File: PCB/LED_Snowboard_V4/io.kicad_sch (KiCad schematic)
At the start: 12 parts, among them J1 Conn_01x04, J3 Conn_01x04, J4 Conn_01x04, J5 XT60PW-M, J6 XT60PW-M, J7 XT60PW-F, J8 Conn_01x03, J9 Conn_01x03, U2 INA220BIDGSR

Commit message: Transfer PCB To Desktop
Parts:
- added D1, D2, D3: D_Schottky, symbol Device:D_Schottky
- added D4, D5: SD05_SOD323, Diode_SMD:D_SOD-323, symbol Diode:SD05_SOD323
- added J10: Conn_01x05, symbol Connector_Generic:Conn_01x05
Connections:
- net +3V3: now also J9.2 (Pin_2)
- net +5V: now also J10.4 (Pin_4)
- net GND: now also J1.1 (Pin_1), J3.1 (Pin_1), J4.1 (Pin_1), J9.3 (Pin_3), D4.1 (A1), D5.1 (A1), J10.5 (Pin_5)
- net SCL: now also D5.2 (A2)
- net SDA: now also D4.2 (A2)
- net VCC: now also J7.2
- net at J8.1 (Pin_1): now also D1.1 (K)
- net at J8.2 (Pin_2): now also D2.1 (K)
- net at J8.3 (Pin_3): now also D3.1 (K)
- net Sensor: now reaches J9.1 (Pin_1)
- new net CLK: J10.1 (Pin_1)
- new net DT: J10.2 (Pin_2)
- new net SW: J10.3 (Pin_3)

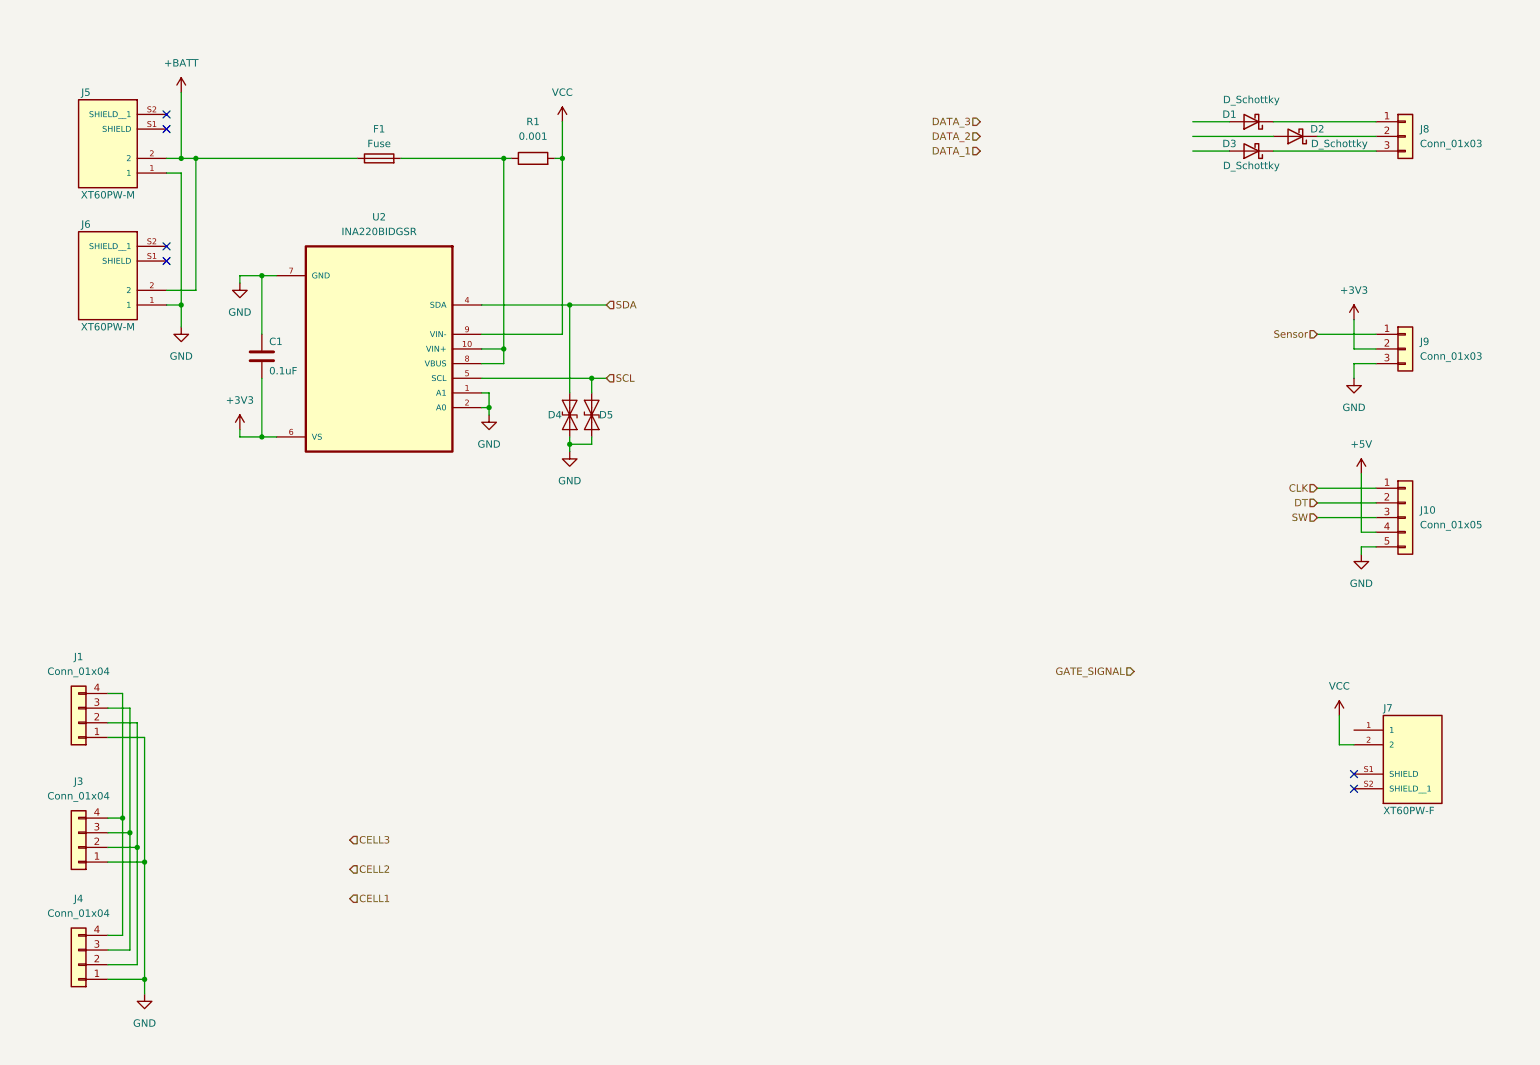
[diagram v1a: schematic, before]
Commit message: Post Review
Reviewed with Tim. need to add power line protections. settled on no battery heater for now
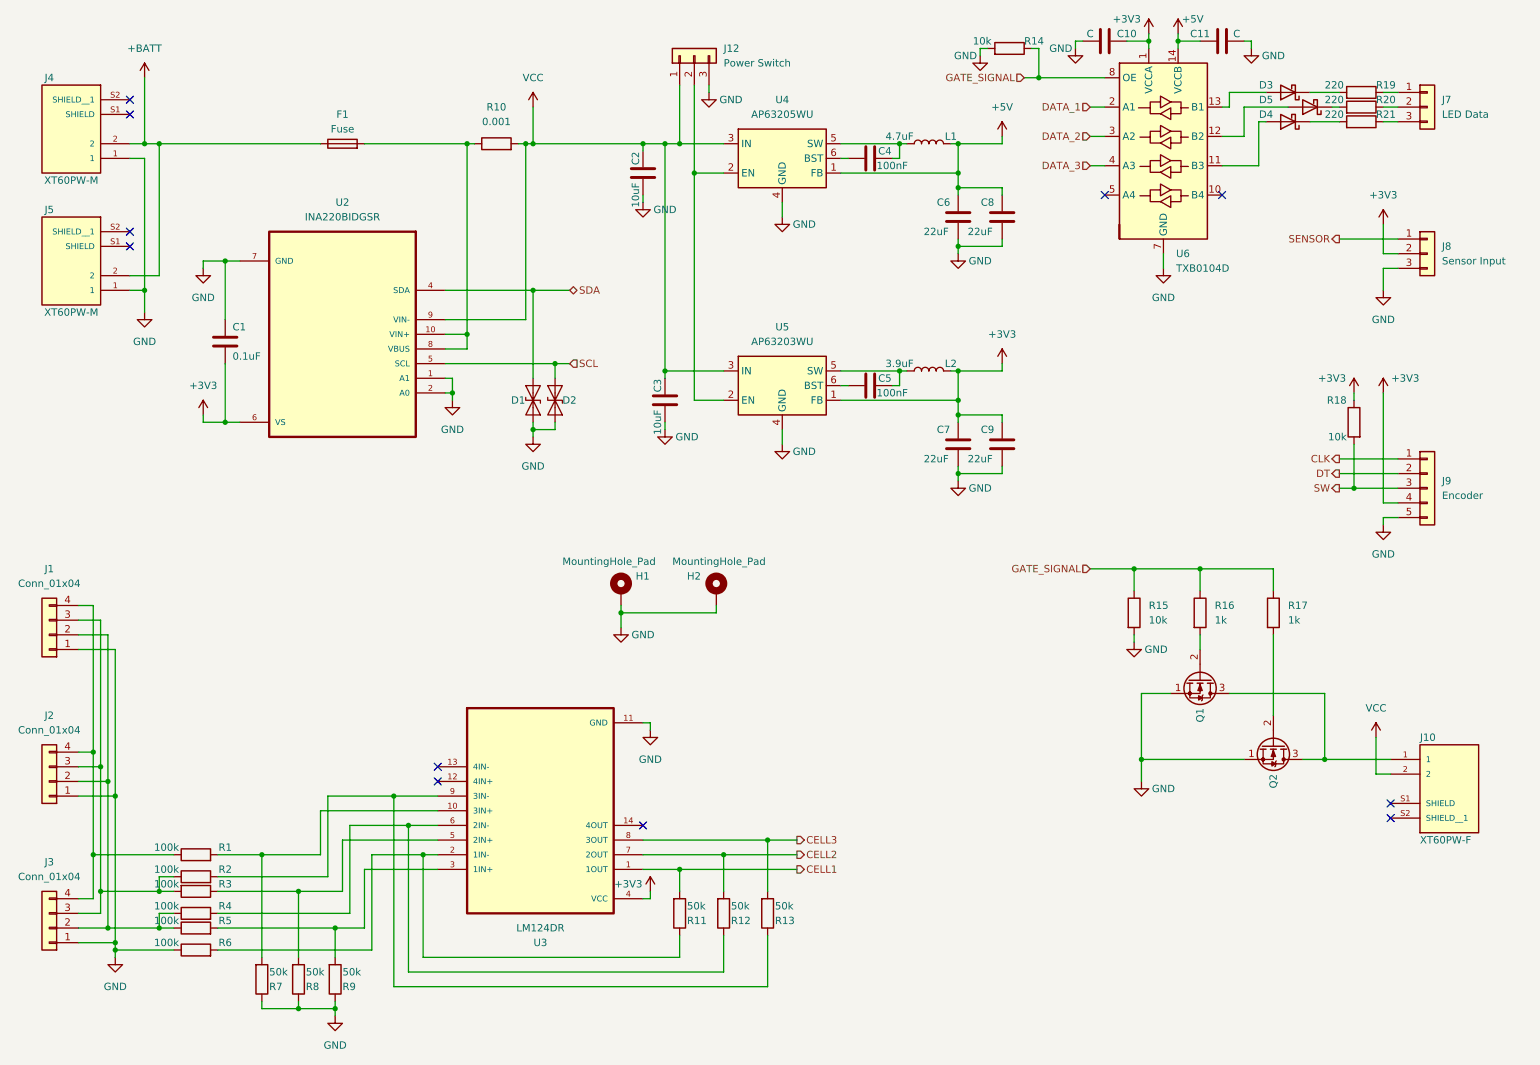
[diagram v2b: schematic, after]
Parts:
- added C10, C11: C, symbol Device:C
- added C2, C3: 10uF, symbol Device:C
- added C4, C5: 100nF, symbol Device:C
- added C6, C7, C8, C9: 22uF, symbol Device:C
- added H1, H2: MountingHole_Pad, symbol Mechanical:MountingHole_Pad
- added J12: Power Switch, symbol Connector_Generic:Conn_01x03
- added L1: 4.7uF, symbol Device:L
- added L2: 3.9uF, symbol Device:L
- added Q1, Q2: ~, symbol Dustins_Symbols:IRFH6200TRPBF
- added R1, R2, R3, R4, R5, R6: 100k, symbol Device:R
- added R11, R12, R13, R7, R8, R9: 50k, symbol Device:R
- added R14, R15, R18: 10k, symbol Device:R
- added R16, R17: 1k, symbol Device:R
- added R19, R20, R21: 220, symbol Device:R
- added U3: LM124DR, SnapEDA Library:SOIC127P600X175-14N, symbol LM124DR:LM124DR
- added U4: AP63205WU, Package_TO_SOT_SMD:TSOT-23-6, symbol Regulator_Switching:AP63205WU
- added U5: AP63203WU, Package_TO_SOT_SMD:TSOT-23-6, symbol Regulator_Switching:AP63203WU
- added U6: TXB0104D, Package_SO:SOIC-14_3.9x8.7mm_P1.27mm, symbol Logic_LevelTranslator:TXB0104D
- J7: renamed from J8; value Conn_01x03 -> LED Data
- J8: renamed from J9; value Conn_01x03 -> Sensor Input
- J9: renamed from J10; value Conn_01x05 -> Encoder
- renumbered D4 to D1, D5 to D2, D1 to D3, D3 to D4, D2 to D5, J7 to J10, J3 to J2, J4 to J3, J5 to J4, J6 to J5, R1 to R10
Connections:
- net +3V3: now also J9.4 (Pin_4), C10.1, C7.2, C9.2, L2.2, R18.1, U3.4 (VCC), U5.1 (FB), U6.1 (VCCA)
- net +5V: now also C11.1, C6.2, C8.2, L1.2, U4.1 (FB), U6.14 (VCCB); no longer J9.4 (Pin_4)
- net CELL1: now also R11.2, U3.1 (1OUT)
- net CELL2: now also R12.2, U3.7 (2OUT)
- net CELL3: now also R13.2, U3.8 (3OUT)
- net DATA_1: now also U6.2 (A1)
- net DATA_2: now also U6.3 (A2)
- net DATA_3: now also U6.4 (A3)
- net GATE_SIGNAL: now also R14.1, R15.1, R16.1, R17.1, U6.8 (OE)
- net GND: now also C10.2, C11.2, C2.1, C3.1, C6.1, C7.1, C8.1, C9.1, H1.1, H2.1, J12.3 (Pin_3), Q1.1 (S), Q2.1 (S), R14.2, R15.2, R6.1, R7.1, R8.1, R9.1, U3.11 (GND), U4.4 (GND), U5.4 (GND), U6.7 (GND)
- net SW: now also R18.2
- net VCC: now also C2.2, C3.2, J12.1 (Pin_1), U4.3 (IN), U5.3 (IN)
- net at J10.1: now also Q1.3 (D), Q2.3 (D)
- net at D3.1 (K): now also R19.2; no longer J7.1 (Pin_1)
- net at D3.2 (A): now also U6.13 (B1)
- net at J7.3 (Pin_3): now also R21.1; no longer D4.1 (K)
- net at D4.2 (A): now also U6.11 (B3)
- net at J7.2 (Pin_2): now also R20.1; no longer D5.1 (K)
- net at D5.2 (A): now also U6.12 (B2)
- net at J1.2 (Pin_2), J2.2 (Pin_2), J3.2 (Pin_2): now also R4.1, R5.1
- net at J1.3 (Pin_3), J2.3 (Pin_3), J3.3 (Pin_3): now also R2.1, R3.2
- net at J1.4 (Pin_4), J2.4 (Pin_4), J3.4 (Pin_4): now also R1.1
- net Sensor renamed SENSOR
- new net: R13.1, R2.2, U3.9 (3IN-)
- new net: R1.2, R7.2, U3.10 (3IN+)
- new net: R11.1, R6.2, U3.2 (1IN-)
- new net: R5.2, R9.2, U3.3 (1IN+)
- new net: R3.1, R8.2, U3.5 (2IN+)
- new net: R12.1, R4.2, U3.6 (2IN-)
- new net: D4.1 (K), R21.2
- new net: Q1.2 (G), R16.2
- new net: Q2.2 (G), R17.2
- new net: D5.1 (K), R20.2
- new net: J12.2 (Pin_2), U4.2 (EN), U5.2 (EN)
- new net: C4.2, L1.1, U4.5 (SW)
- new net: C4.1, U4.6 (BST)
- new net: C5.1, U5.6 (BST)
- new net: C5.2, L2.1, U5.5 (SW)
- new net: J7.1 (Pin_1), R19.1
- no-connect marks 6 -> 11
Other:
- moved on the sheet: C1, D1, D2, D3, D4, D5, F1, J1, J10, J2, J3, J4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
